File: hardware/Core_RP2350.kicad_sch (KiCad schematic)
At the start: 73 parts, among them J1 5-146281-3, J2 5-146281-3, J3 AudioJack3, J4 USB_C_Receptacle_USB2.0, J5 Micro_SD_Card_Det_Hirose_DM3AT, SW1 SPST-NO, SW2 SPST-NO, SW3 SPST-NO, U2 W25Q16JVUXIQ, U3 ADUM4160, U32 RP2350_80QFN

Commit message: update pcb draft
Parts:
- removed C4: 10uF, Capacitor_SMD:C_0603_1608Metric, symbol harp.device.quad.dac:C_0603
- removed R19: 100, Resistor_SMD:R_0603_1608Metric, symbol harp.device.quad.dac:R_0603
- removed R22: 10K, Resistor_SMD:R_0402_1005Metric, symbol harp.device.quad.dac:R_0603
- removed SW3: SPST-NO, kicad-lib:SW_Push_1P1T-SH_NO_Vertical_Wuerth_WS-TASV, symbol harp.device.quad.dac:SW_Push_with_gnd
- added C5, C9: 100nF, Capacitor_SMD:C_0402_1005Metric, symbol harp.device.quad.dac:C_0603
- added C8: 4.7uF, Capacitor_SMD:C_0603_1608Metric, symbol harp.device.quad.dac:C_0603
- added D29: TPD6E004, kicad-lib:IC_TPD6E004RSER, symbol kicad-lib:TPD6E004
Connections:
- net +1V1: now also C8.1, C9.2
- net +3.3V: now also C5.1, D29.8 (Vcc)
- net GND: now also C5.2, C8.2, C9.1, D29.4 (GND)
- net SD_CLK: now also D29.1 (K1)
- net SD_CMD: now also D29.7 (K6)
- net SD_DAT0: now also D29.2 (K2)
- net SD_DAT1: now also D29.3 (K3)
- net SD_DAT2: now also D29.5 (K4)
- net SD_DAT3: now also D29.6 (K5)
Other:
- note added: "near DVDD pins"
- note removed: "Extra Button"

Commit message: update pcb
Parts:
- removed C3: 10uF, Capacitor_SMD:C_0603_1608Metric, symbol harp.device.quad.dac:C_0603
- removed R1: 100, Resistor_SMD:R_0603_1608Metric, symbol harp.device.quad.dac:R_0603
- removed R4: 10K, Resistor_SMD:R_0402_1005Metric, symbol harp.device.quad.dac:R_0603
- removed SW1: SPST-NO, kicad-lib:SW_Push_1P1T-SH_NO_Vertical_Wuerth_WS-TASV, symbol harp.device.quad.dac:SW_Push_with_gnd
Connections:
- net +3.3V: now also U32.35 (RUN)
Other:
- note removed: "Reset"

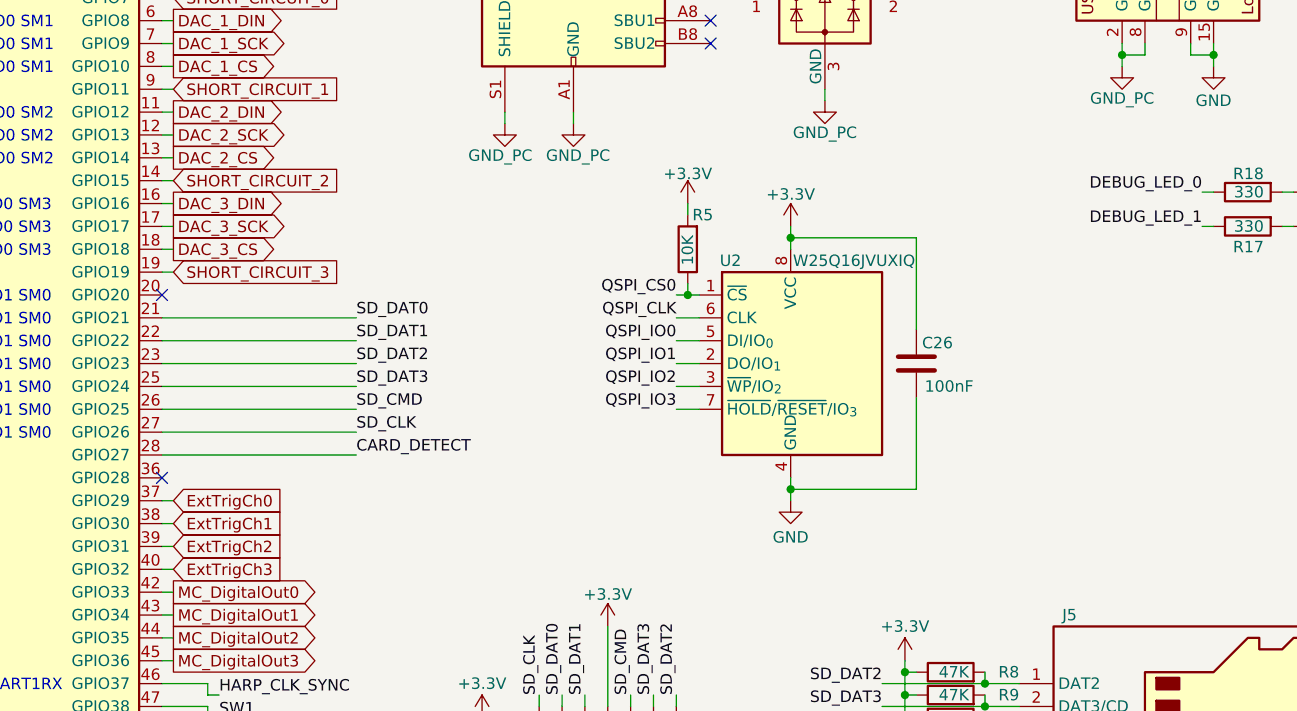
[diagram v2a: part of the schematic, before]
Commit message: fix sd card order; finish pcb draft
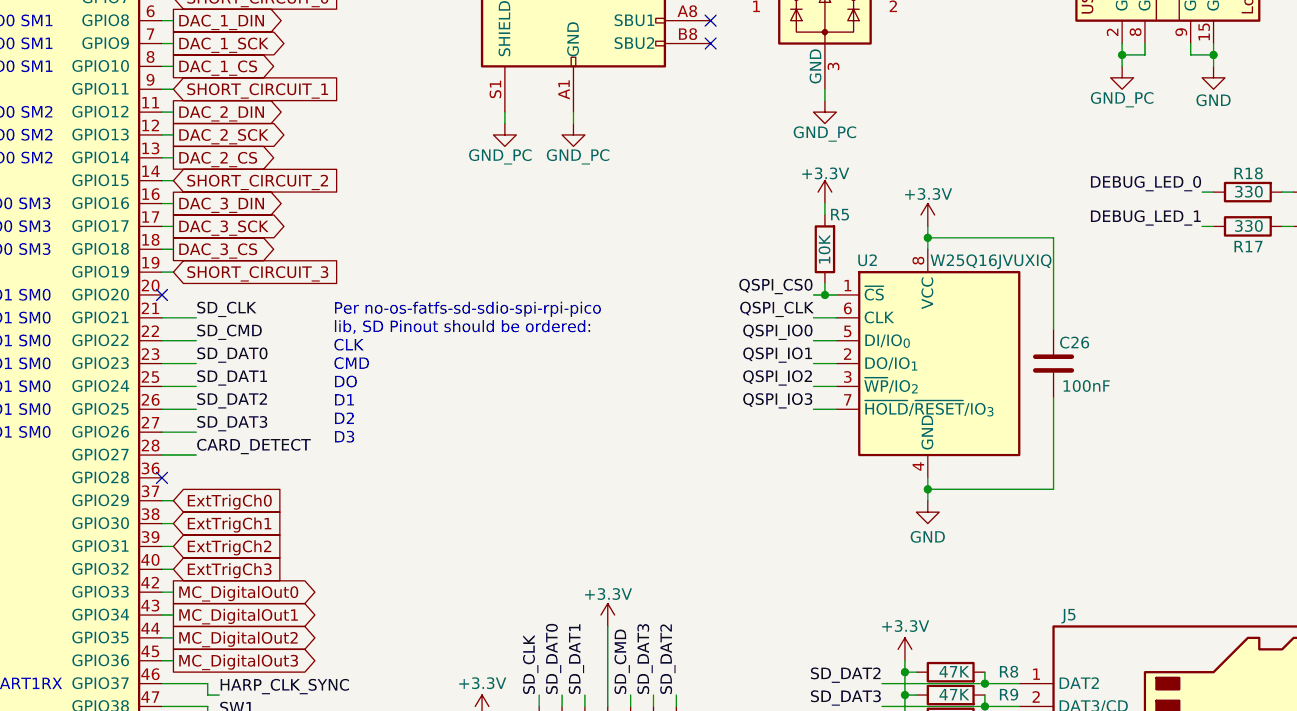
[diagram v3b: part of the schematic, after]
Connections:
- net SD_CLK: now also U32.21 (GPIO21); no longer U32.27 (GPIO26)
- net SD_CMD: now also U32.22 (GPIO22); no longer U32.26 (GPIO25)
- net SD_DAT0: now also U32.23 (GPIO23); no longer U32.21 (GPIO21)
- net SD_DAT1: now also U32.25 (GPIO24); no longer U32.22 (GPIO22)
- net SD_DAT2: now also U32.26 (GPIO25); no longer U32.23 (GPIO23)
- net SD_DAT3: now also U32.27 (GPIO26); no longer U32.25 (GPIO24)
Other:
- note added: "Per no-os-fatfs-sd-sdio-spi-rpi-pico lib, SD Pinout should be ordered: CLK CMD DO D1 D2 D3"
- moved on the sheet: C26, R5, U2

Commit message: update bom
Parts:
- removed R17, R18: 330, Resistor_SMD:R_0603_1608Metric, symbol harp.device.quad.dac:R_0603
- added R17, R18: 1K, Resistor_SMD:R_0402_1005Metric, symbol Device:R
- R10, R11, R12, R13, R14, R8, R9: Link (none) -> https://www.digikey.com/en/products/detail/yageo/RC0402FR-0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; Manufacturer (none) -> YAGEO; Manufacturer Number (none) -> RC0402FR-0747KL
- R2: Link (none) -> https://www.digikey.com/en/products/detail/panasonic-electr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; Manufacturer (none) -> Panasonic Electronic Components; Manufacturer Number (none) -> ERJ-2RKF1001X
- R5: Link (none) -> https://www.digikey.com/en/products/detail/samsung-electro-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; Manufacturer (none) -> Samsung Electro-Mechanics; Manufacturer Number (none) -> RC1005F103CS
- R6, R7: Link (none) -> https://www.digikey.com/en/products/detail/yageo/RC0402FR-0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; Manufacturer (none) -> YAGEO; Manufacturer Number (none) -> RC0402FR-075K1L
- SW2: Manufacturer Number (none) -> 435451019820
- U32: Link (none) -> https://www.digikey.com/en/products/detail/raspberry-pi/SC1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; Manufacturer (none) -> Raspberry Pi; Manufacturer Number (none) -> SC1510-A4
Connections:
- net DEBUG_LED_0: now also R17.2
- net DEBUG_LED_1: now also R18.2
- net at LED1.2 (A): now also R18.1
- net at LED2.2 (A): now also R17.1
- net QSPI_CS0 renamed QSPI_CS

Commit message: update bom
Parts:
- J1, J2: Alternate n/a -> (none); Link n/a -> https://www.digikey.com/en/products/detail/te-connectivity-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; Manufacturer n/a -> TE Connectivity AMP Connectors; Manufacturer Number n/a -> 5-146281-3; Notes DNP -> (none)

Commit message: update footprints to meet min pad clearance of 0.2mm
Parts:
- FID1, FID2, FID3: footprint harp.device.quad.dac.kicad:Fiducial_0.5mm_Mask1mm -> Fiducial:Fiducial_0.5mm_Mask1mm
- L1: footprint kicad_component_library:L_0806_2016Metric -> kicad-lib:L_0806_2016Metric
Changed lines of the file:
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@@
 			)
 		)
-		(property "Footprint" "harp.device.quad.dac.kicad:Fiducial_0.5mm_Mask1mm"
+		(property "Footprint" "Fiducial:Fiducial_0.5mm_Mask1mm"
 			(at 162.56 195.58 0)
 			(effects
@@
 			)
 		)
-		(property "Footprint" "harp.device.quad.dac.kicad:Fiducial_0.5mm_Mask1mm"
+		(property "Footprint" "Fiducial:Fiducial_0.5mm_Mask1mm"
 			(at 167.64 195.58 0)
 			(effects
@@
 			)
 		)
-		(property "Footprint" "harp.device.quad.dac.kicad:Fiducial_0.5mm_Mask1mm"
+		(property "Footprint" "Fiducial:Fiducial_0.5mm_Mask1mm"
 			(at 172.72 195.58 0)
 			(effects
@@
 			)
 		)
-		(property "Footprint" "kicad_component_library:L_0806_2016Metric"
+		(property "Footprint" "kicad-lib:L_0806_2016Metric"
 			(at 58.42 43.18 0)
 			(effects

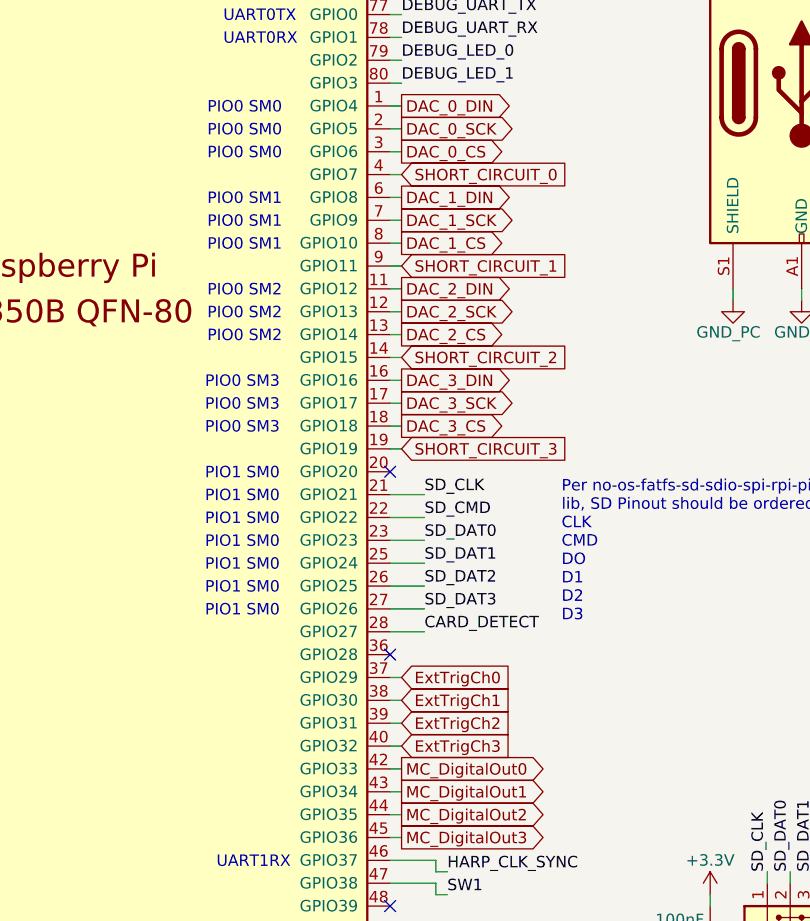
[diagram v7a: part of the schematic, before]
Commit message: feat pcba updates (#69)
* replace INA181 w INA630

* flip c12; put ext triggers on gpio multiple of 8

* add pulldowns to external triggers

* change R3, R15, R16, R20, R21 package to 0402

* update 1K, 31K6, 10K resistors to 0.1%

* swap BNC connectors to taller versions

* move short-circuit pins to fall within multiple of 8 boundary

* add 1.0/1.1 hw pinout to config with default as 1.0

* update hardware author
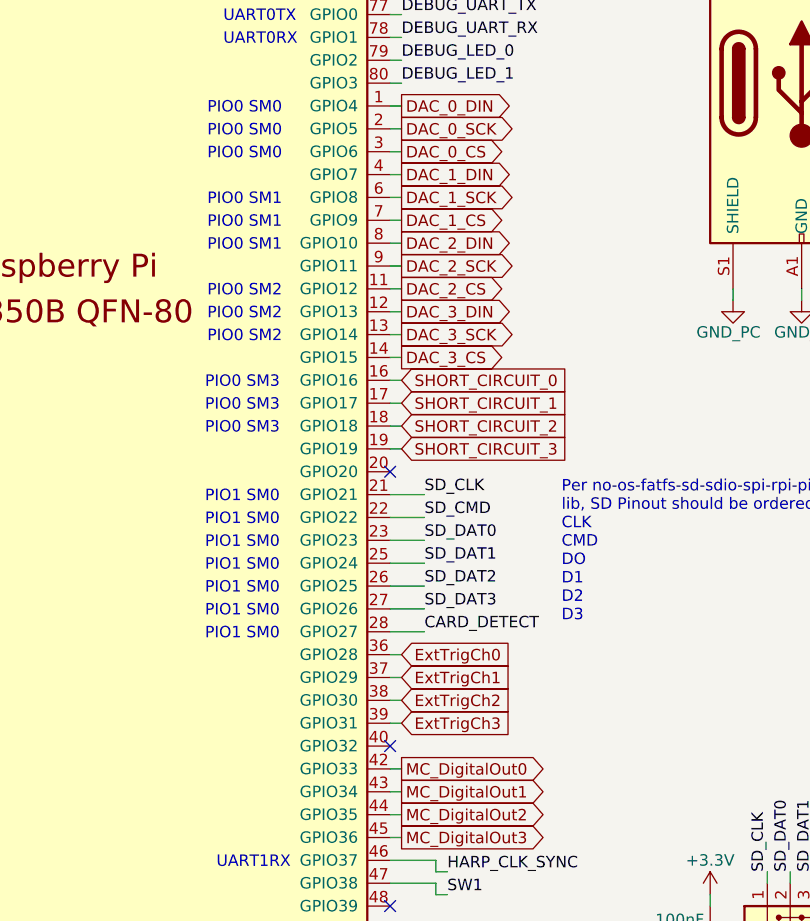
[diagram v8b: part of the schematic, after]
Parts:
- R15, R16, R20, R21, R3: footprint Resistor_SMD:R_0603_1608Metric -> Resistor_SMD:R_0402_1005Metric
- R17, R18: Link https://www.digikey.com/en/products/detail/panasonic-electr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 -> https://www.digikey.com/en/products/detail/yageo/RT0402BRE0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; Manufacturer Panasonic Electronic Components -> YAGEO; Manufacturer Number ERJ-2RKF1001X -> RT0402BRE071KL; Tolerance (none) -> 0.1%
- R2: Link https://www.digikey.com/en/products/detail/panasonic-electr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 -> https://www.digikey.com/en/products/detail/yageo/RT0402BRE0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; Manufacturer Panasonic Electronic Components -> YAGEO; Manufacturer Number ERJ-2RKF1001X -> RT0402BRE071KL
- R5: Link https://www.digikey.com/en/products/detail/samsung-electro-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 -> https://www.digikey.com/en/products/detail/yageo/RT0402BRD0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; Manufacturer Samsung Electro-Mechanics -> YAGEO; Manufacturer Number RC1005F103CS -> RT0402BRD0710KL
- R76, R77: PCBWay Link https://www.pcbway.com/components/detail/RC0402FR0727RL/656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 -> (none)
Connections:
- net DAC_1_CS: now also U32.7 (GPIO9); no longer U32.8 (GPIO10)
- net DAC_1_DIN: now also U32.4 (GPIO7); no longer U32.6 (GPIO8)
- net DAC_1_SCK: now also U32.6 (GPIO8); no longer U32.7 (GPIO9)
- net DAC_2_CS: now also U32.11 (GPIO12); no longer U32.13 (GPIO14)
- net DAC_2_DIN: now also U32.8 (GPIO10); no longer U32.11 (GPIO12)
- net DAC_2_SCK: now also U32.9 (GPIO11); no longer U32.12 (GPIO13)
- net DAC_3_CS: now also U32.14 (GPIO15); no longer U32.18 (GPIO18)
- net DAC_3_DIN: now also U32.12 (GPIO13); no longer U32.16 (GPIO16)
- net DAC_3_SCK: now also U32.13 (GPIO14); no longer U32.17 (GPIO17)
- net ExtTrigCh0: now also U32.36 (GPIO28); no longer U32.37 (GPIO29)
- net ExtTrigCh1: now also U32.37 (GPIO29); no longer U32.38 (GPIO30)
- net ExtTrigCh2: now also U32.38 (GPIO30); no longer U32.39 (GPIO31)
- net ExtTrigCh3: now also U32.39 (GPIO31); no longer U32.40 (GPIO32)
- net SHORT_CIRCUIT_0: now also U32.16 (GPIO16); no longer U32.4 (GPIO7)
- net SHORT_CIRCUIT_1: now also U32.17 (GPIO17); no longer U32.9 (GPIO11)
- net SHORT_CIRCUIT_2: now also U32.18 (GPIO18); no longer U32.14 (GPIO15)
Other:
- title: harp.device.quad-dac -> harp device quad dac
